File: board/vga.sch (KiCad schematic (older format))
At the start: 19 parts, among them P501 VGA RX I2C 3v, P502 VGA TX I2C 3v, P503 VGA RX I2C 5v, P504 VGA TX I2C 5v, P505 DE-15, P506 DE-15, P601 3-RCA, U501 TCA9617A, U502 TCA9617A

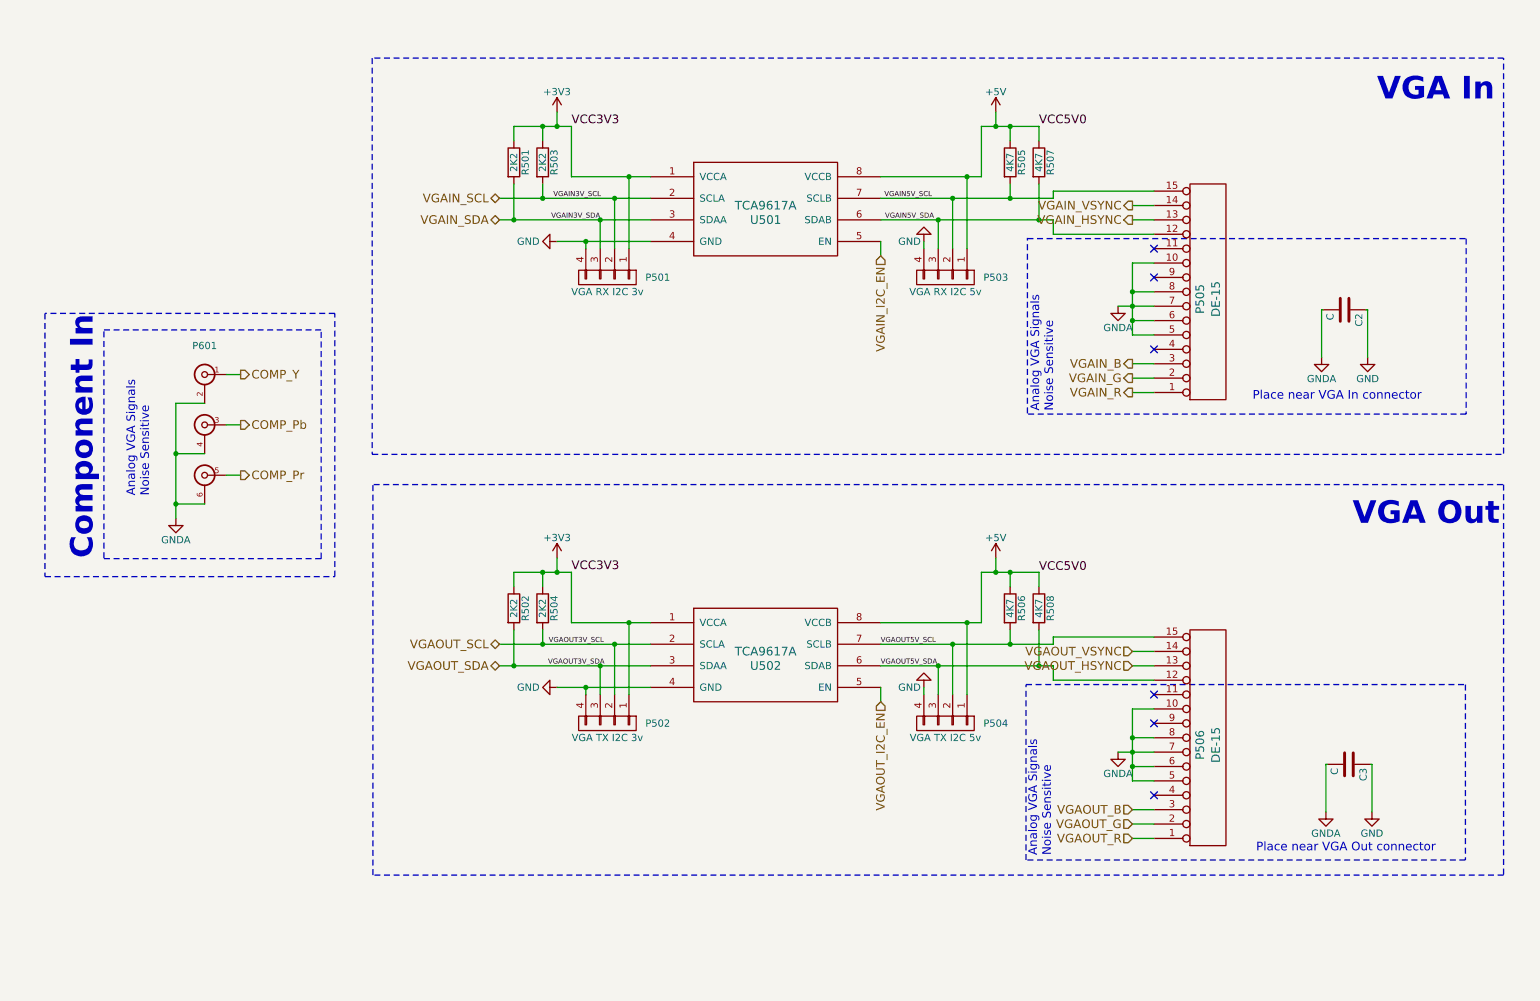
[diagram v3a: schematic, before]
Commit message: Giving things better names.
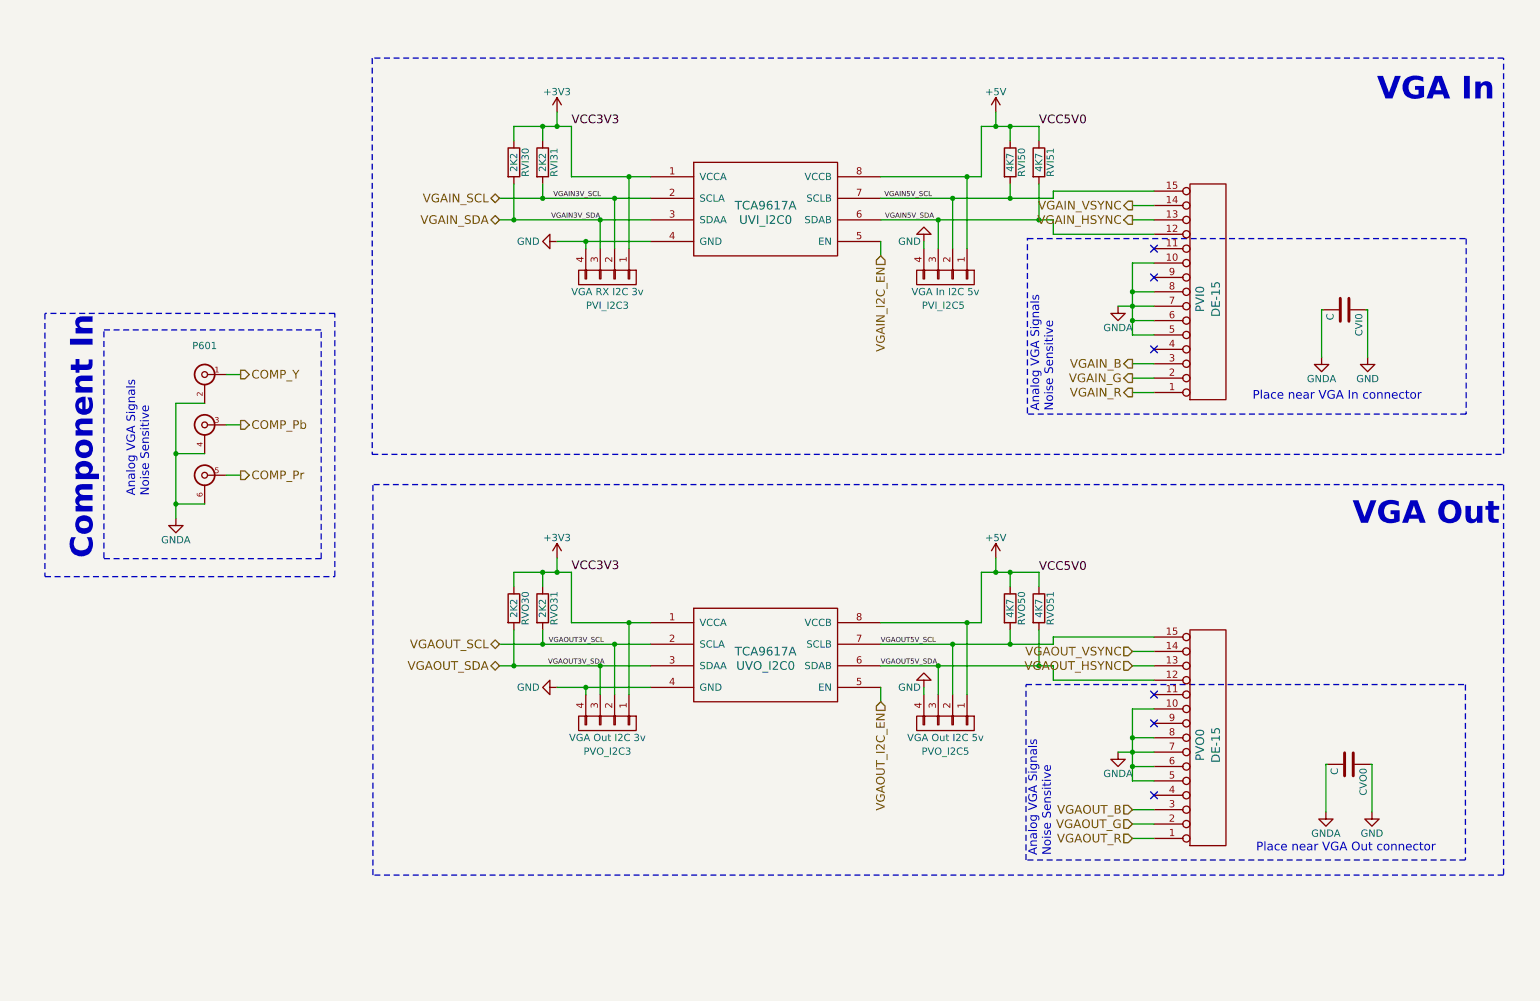
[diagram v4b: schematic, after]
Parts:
- PVI_I2C5: renamed from P503; value VGA RX I2C 5v -> VGA In I2C 5v
- PVO_I2C3: renamed from P502; value VGA TX I2C 3v -> VGA Out I2C 3v
- PVO_I2C5: renamed from P504; value VGA TX I2C 5v -> VGA Out I2C 5v
- renumbered C2 to CVI0, C3 to CVO0, P505 to PVI0, P501 to PVI_I2C3, P506 to PVO0, R501 to RVI30, R503 to RVI31, R505 to RVI50, R507 to RVI51, R502 to RVO30, R504 to RVO31, R506 to RVO50, R508 to RVO51, U501 to UVI_I2C0, U502 to UVO_I2C0
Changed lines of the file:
@@
 VGAOUT_SDA
 $Comp
-L TCA9617A U502
+L TCA9617A UVO_I2C0
 U 1 1 53BEC842
 P 5750 5000
-F 0 "U502" H 5750 4950 60  0000 C CNN
+F 0 "UVO_I2C0" H 5750 4950 60  0000 C CNN
 F 1 "TCA9617A" H 5750 5050 60  0000 C CNN
 F 2 "Housings_SSOP:MSOP-8_3x3mm_Pitch0.65mm" H 6000 5100 60  0001 C CNN
@@
 $EndComp
 $Comp
-L DE-15 P506
+L DE-15 PVO0
 U 1 1 563F19C1
 P 8800 5600
-F 0 "P506" V 8770 5600 60  0000 C CNN
+F 0 "PVO0" V 8770 5600 60  0000 C CNN
 F 1 "DE-15" V 8880 5600 60  0000 C CNN
 F 2 "DE-15:TE-1-1734530-1" H 8800 5600 60  0001 C CNN
@@
 VGAOUT_VSYNC
 $Comp
-L R R508
+L R RVO51
 U 1 1 56419F6C
 P 7650 4650
-F 0 "R508" V 7730 4650 50  0000 C CNN
+F 0 "RVO51" V 7730 4650 50  0000 C CNN
 F 1 "4K7" V 7650 4650 50  0000 C CNN
 F 2 "Resistors_SMD:R_0805_HandSoldering" V 7580 4650 30  0001 C CNN
@@
 $EndComp
 $Comp
-L R R506
+L R RVO50
 U 1 1 5641A01D
 P 7450 4650
-F 0 "R506" V 7530 4650 50  0000 C CNN
+F 0 "RVO50" V 7530 4650 50  0000 C CNN
 F 1 "4K7" V 7450 4650 50  0000 C CNN
 F 2 "Resistors_SMD:R_0805_HandSoldering" V 7380 4650 30  0001 C CNN
@@
 $EndComp
 $Comp
-L R R504
+L R RVO31
 U 1 1 5641A1E0
 P 4200 4650
-F 0 "R504" V 4280 4650 50  0000 C CNN
+F 0 "RVO31" V 4280 4650 50  0000 C CNN
 F 1 "2K2" V 4200 4650 50  0000 C CNN
 F 2 "Resistors_SMD:R_0805_HandSoldering" V 4130 4650 30  0001 C CNN
@@
 $EndComp
 $Comp
-L R R502
+L R RVO30
 U 1 1 5641A20F
 P 4000 4650
-F 0 "R502" V 4080 4650 50  0000 C CNN
+F 0 "RVO30" V 4080 4650 50  0000 C CNN
 F 1 "2K2" V 4000 4650 50  0000 C CNN
 F 2 "Resistors_SMD:R_0805_HandSoldering" V 3930 4650 30  0001 C CNN
@@
 VGAIN_SDA
 $Comp
-L TCA9617A U501
+L TCA9617A UVI_I2C0
 U 1 1 5641B8BE
 P 5750 1900
-F 0 "U501" H 5750 1850 60  0000 C CNN
+F 0 "UVI_I2C0" H 5750 1850 60  0000 C CNN
 F 1 "TCA9617A" H 5750 1950 60  0000 C CNN
 F 2 "Housings_SSOP:MSOP-8_3x3mm_Pitch0.65mm" H 6000 2000 60  0001 C CNN
@@
 $EndComp
 $Comp
-L DE-15 P505
+L DE-15 PVI0
 U 1 1 5641B8C8
 P 8800 2500
-F 0 "P505" V 8770 2500 60  0000 C CNN
+F 0 "PVI0" V 8770 2500 60  0000 C CNN
 F 1 "DE-15" V 8880 2500 60  0000 C CNN
 F 2 "DE-15:TE-1-1734530-1" H 8800 2500 60  0001 C CNN
@@
 VGAIN_VSYNC
 $Comp
-L R R507
+L R RVI51
 U 1 1 5641B8F6
 P 7650 1550
-F 0 "R507" V 7730 1550 50  0000 C CNN
+F 0 "RVI51" V 7730 1550 50  0000 C CNN
 F 1 "4K7" V 7650 1550 50  0000 C CNN
 F 2 "Resistors_SMD:R_0805_HandSoldering" V 7580 1550 30  0001 C CNN
@@
 $EndComp
 $Comp
-L R R505
+L R RVI50
 U 1 1 5641B8FC
 P 7450 1550
-F 0 "R505" V 7530 1550 50  0000 C CNN
+F 0 "RVI50" V 7530 1550 50  0000 C CNN
 F 1 "4K7" V 7450 1550 50  0000 C CNN
 F 2 "Resistors_SMD:R_0805_HandSoldering" V 7380 1550 30  0001 C CNN
@@
 $EndComp
 $Comp
-L R R503
+L R RVI31
 U 1 1 5641B902
 P 4200 1550
-F 0 "R503" V 4280 1550 50  0000 C CNN
+F 0 "RVI31" V 4280 1550 50  0000 C CNN
 F 1 "2K2" V 4200 1550 50  0000 C CNN
 F 2 "Resistors_SMD:R_0805_HandSoldering" V 4130 1550 30  0001 C CNN
@@
 $EndComp
 $Comp
-L R R501
+L R RVI30
 U 1 1 5641B908
 P 4000 1550
-F 0 "R501" V 4080 1550 50  0000 C CNN
+F 0 "RVI30" V 4080 1550 50  0000 C CNN
 F 1 "2K2" V 4000 1550 50  0000 C CNN
 F 2 "Resistors_SMD:R_0805_HandSoldering" V 3930 1550 30  0001 C CNN
@@
 $EndComp
 $Comp
-L CONN_01X04 P501
+L CONN_01X04 PVI_I2C3
 U 1 1 5692AE99
 P 4650 2350
-F 0 "P501" V 4650 2700 50  0000 C CNN
+F 0 "PVI_I2C3" V 4845 2350 50  0000 C CNN
 F 1 "VGA RX I2C 3v" V 4750 2350 50  0000 C CNN
 F 2 "CON-SMD-2.54:HARWIN-M20-87-4x1" H 4650 2350 50  0001 C CNN
@@
 $EndComp
 $Comp
-L CONN_01X04 P502
+L CONN_01X04 PVO_I2C3
 U 1 1 5692BCA4
 P 4650 5450
-F 0 "P502" V 4650 5800 50  0000 C CNN
-F 1 "VGA TX I2C 3v" V 4750 5450 50  0000 C CNN
+F 0 "PVO_I2C3" V 4845 5450 50  0000 C CNN
+F 1 "VGA Out I2C 3v" V 4750 5450 50  0000 C CNN
 F 2 "CON-SMD-2.54:HARWIN-M20-87-4x1" H 4650 5450 50  0001 C CNN
 F 3 "" H 4650 5450 50  0000 C CNN
@@
 $EndComp
 $Comp
-L CONN_01X04 P503
+L CONN_01X04 PVI_I2C5
 U 1 1 5692C534
 P 7000 2350
-F 0 "P503" V 7000 2700 50  0000 C CNN
-F 1 "VGA RX I2C 5v" V 7100 2350 50  0000 C CNN
+F 0 "PVI_I2C5" V 7195 2335 50  0000 C CNN
+F 1 "VGA In I2C 5v" V 7100 2350 50  0000 C CNN
 F 2 "CON-SMD-2.54:HARWIN-M20-87-4x1" H 7000 2350 50  0001 C CNN
 F 3 "" H 7000 2350 50  0000 C CNN
@@
 $EndComp
 $Comp
-L CONN_01X04 P504
+L CONN_01X04 PVO_I2C5
 U 1 1 5692D0C0
 P 7000 5450
-F 0 "P504" V 7000 5800 50  0000 C CNN
-F 1 "VGA TX I2C 5v" V 7100 5450 50  0000 C CNN
+F 0 "PVO_I2C5" V 7195 5450 50  0000 C CNN
+F 1 "VGA Out I2C 5v" V 7100 5450 50  0000 C CNN
 F 2 "CON-SMD-2.54:HARWIN-M20-87-4x1" H 7000 5450 50  0001 C CNN
 F 3 "" H 7000 5450 50  0000 C CNN
@@
 $EndComp
 $Comp
-L C C2
+L C CVI0
 U 1 1 579C5DC0
 P 9775 2575
-F 0 "C2" H 9800 2675 50  0000 L CNN
+F 0 "CVI0" H 9800 2675 50  0000 L CNN
 F 1 "C" H 9800 2475 50  0000 L CNN
 F 2 "Capacitors_SMD:C_1206_HandSoldering" H 9813 2425 50  0001 C CNN
@@
 $EndComp
 $Comp
-L C C3
+L C CVO0
 U 1 1 579C6016
 P 9805 5735
-F 0 "C3" H 9830 5835 50  0000 L CNN
+F 0 "CVO0" H 9830 5835 50  0000 L CNN
 F 1 "C" H 9830 5635 50  0000 L CNN
 F 2 "Capacitors_SMD:C_1206_HandSoldering" H 9843 5585 50  0001 C CNN
